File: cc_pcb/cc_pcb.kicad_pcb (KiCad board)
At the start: 2 copper layers, 134.7 x 117.2 mm, 66 parts, among them J1 Conn_02x05_Odd_Even, J10 AC-DC Converter, J2 Wi-Fi Module, J3 Controller (40Pin->SPI), J4 RFID Scanner, J5 4x4 Keypad, J6 SD Reader, J7 PS_Modules, J8 PS_Designed, J9 DC-DC Converter, Q1 2SC1941, SW1 SW_Push, U1 STM32F091RCTx, U2 LM393, U3 LD1117S33TR_SOT223, U4 LM2576T-5

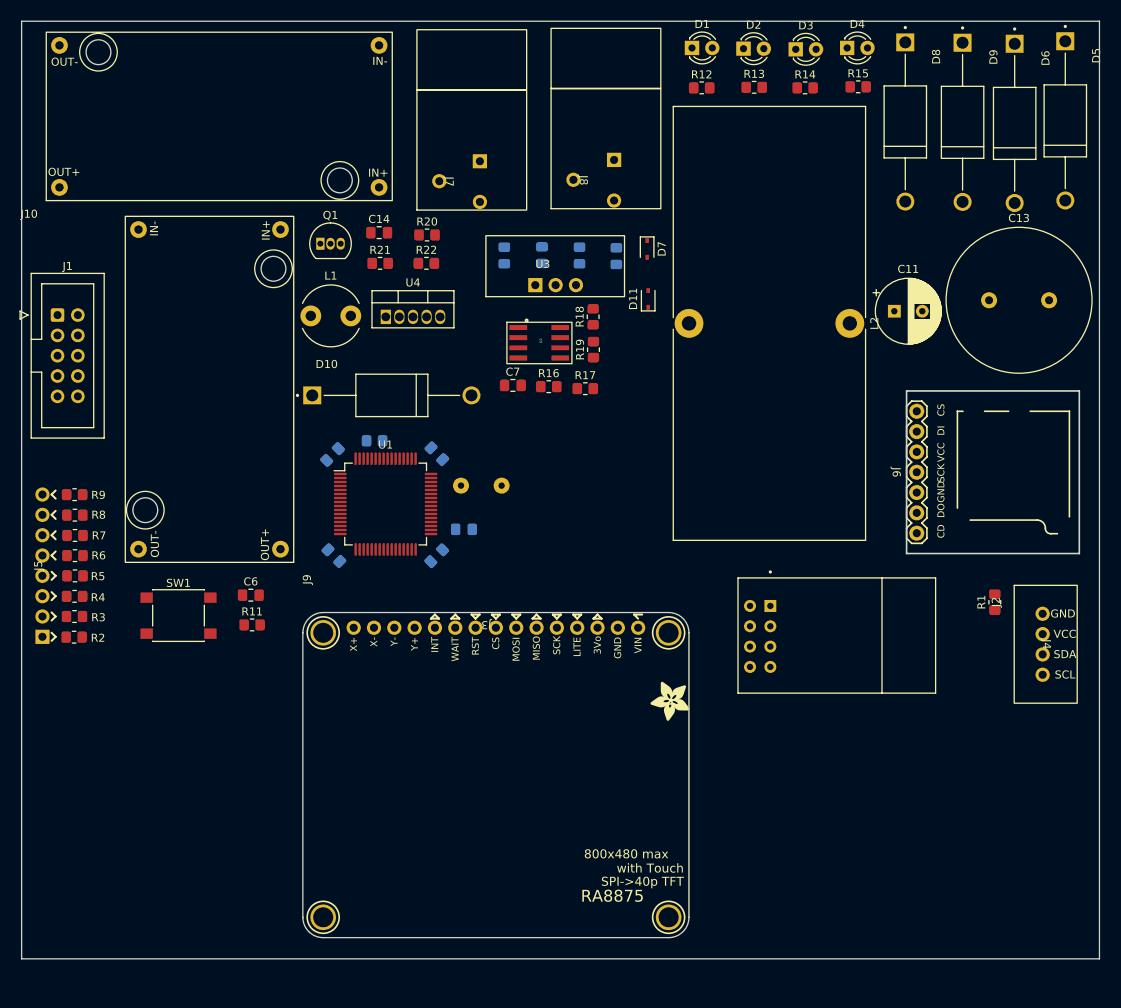
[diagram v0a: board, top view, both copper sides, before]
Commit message: RA8875 and ESP8266 updated footprints
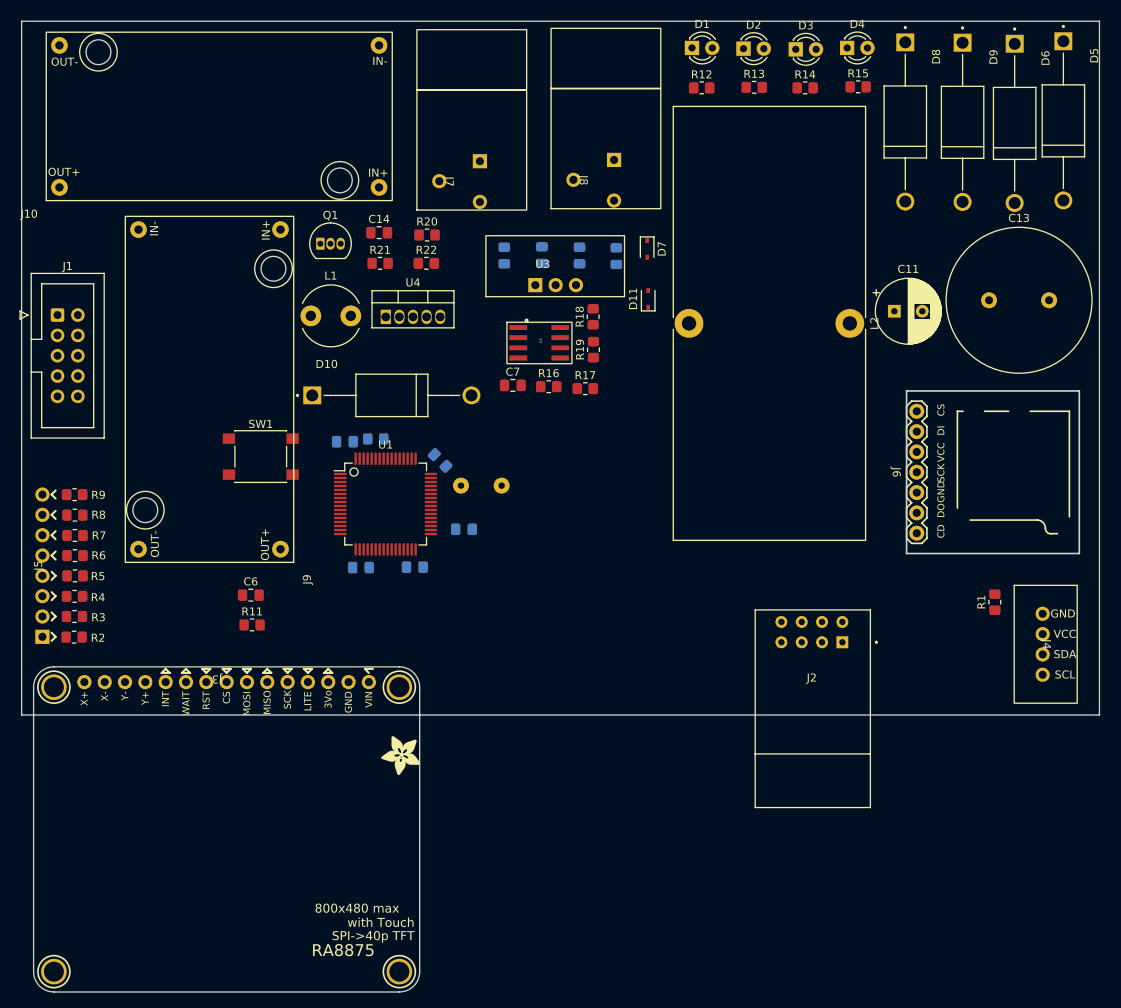
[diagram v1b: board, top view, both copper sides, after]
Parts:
- moved J3 34.3 mm to (105.3, 118.1)
- moved SW1 22.4 mm to (110.8, 90.8)
- moved J2 9.56 mm to (179.7, 122.3), turned to 180 degrees
- moved C1 3.69 mm to (123.3, 104.7), turned to 180 degrees
- moved C4 3.09 mm to (130.0, 104.6), turned to 180 degrees
- moved C2 2.22 mm to (121.3, 89.0), turned to 0 degrees
- moved C3 0.94 mm to (133.2, 91.3), turned to -45 degrees
- moved R10 0.28 mm to (125.1, 88.6)
- moved D5 0.24 mm to (211.1, 48.8)
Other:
- board size 134.7 x 117.2 mm -> 134.7 x 86.7 mm

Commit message: micro sd connector schematic/footprint, lm324 footprint
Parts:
- removed D10: 1N5822, imported_footprints:DIO_1N5822
- removed J4: RFID Scanner, imported_footprints:RFID_Reader_PCB
- removed Q1: 2SC1941, Package_TO_SOT_THT:TO-92_Inline
- added C15: 100nF, Capacitor_SMD:C_0805_2012Metric_Pad1.18x1.45mm_HandSolder, F.Cu at (35.2, 111.5)
- added C16: 33pF, Capacitor_SMD:C_0805_2012Metric_Pad1.18x1.45mm_HandSolder, F.Cu at (76.1, 27.0)
- added C17: 22uF, Capacitor_SMD:C_0805_2012Metric_Pad1.18x1.45mm_HandSolder, F.Cu at (71.3, 30.0)
- added C18: 100nF, Capacitor_SMD:C_0805_2012Metric_Pad1.18x1.45mm_HandSolder, F.Cu at (19.4, 120.5)
- added C19: .1uF, Capacitor_SMD:C_0805_2012Metric_Pad1.18x1.45mm_HandSolder, F.Cu at (76.1, 24.0)
- added C20: 10uF, Capacitor_SMD:C_0805_2012Metric_Pad1.18x1.45mm_HandSolder, F.Cu at (71.3, 24.0)
- added C21: .1uF, Capacitor_SMD:C_0805_2012Metric_Pad1.18x1.45mm_HandSolder, F.Cu at (71.3, 27.0)
- added J11: 2.8in SPI TFT Touch Display, imported_footprints:tft_2.8in_touch_display, F.Cu at (111.0, 117.3)
- added R23: 220k, Resistor_SMD:R_0805_2012Metric_Pad1.20x1.40mm_HandSolder, F.Cu at (71.3, 33.0)
- added R24: 30k, Resistor_SMD:R_0805_2012Metric_Pad1.20x1.40mm_HandSolder, F.Cu at (80.9, 24.0)
- added U6: RFID_Scanner, imported_footprints:RFID_Reader_PCB, F.Cu at (210.2, 114.5)
- C14: value 22uF -> 10uF
- FB1: footprint Ferrite_THT:LairdTech_28C0236-0JW-10 -> Resistor_SMD:R_0805_2012Metric_Pad1.20x1.40mm_HandSolder
- L1: value INDUCTOR -> 2.2uH
- R20: value 10k -> 100k
- R21: value 10k -> 11.3k
- U2: value LM393 -> LM324; footprint imported_footprints:LM393 -> imported_footprints:LM324
- U4: value LM2576T-5 -> TPS56325x; footprint Package_TO_SOT_THT:TO-220-5_Vertical -> imported_footprints:TPS56325x
- moved J2 82.8 mm to (248.6, 76.4)
- moved J3 58.4 mm to (163.6, 116.6)
- moved SW1 22.7 mm to (131.6, 81.8)
- moved FB1 20.8 mm to (123.8, 106.3), turned to 135 degrees
- moved C2 20.3 mm to (139.0, 98.9), turned to -135 degrees
- moved R10 17.5 mm to (136.5, 101.9), turned to 45 degrees
- moved C1 15.8 mm to (126.5, 89.2), turned to 45 degrees
- moved C5 15.5 mm to (120.8, 101.7), turned to 45 degrees
- moved C3 15.0 mm to (128.9, 105.7), turned to 180 degrees
- moved C4 13.5 mm to (121.8, 94.0), turned to 45 degrees
- moved R1 8.28 mm to (203.4, 117.2)
- moved U1 3.54 mm to (129.9, 97.0), turned to -135 degrees
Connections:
- net /BOOT0 renamed PF11
- net /CD renamed /SD_CD
- net /GPIO-0 renamed /ESP_GPIO-0
- net /GPIO-2 renamed /ESP_GPIO-2
- net /LITE renamed /7_LITE
- net /WAIT renamed /7_WAIT
- C1 pad 1: +3V3 -> 3.3V
- C1 pad 2: GND -> 3.3V
- C11 pad 2: 7.5_GND -> 3.3V
- C13 pad 2: 7.5_GND -> 3.3V
- C14 pad 1: +3V3 -> +7.5V
- C14 pad 2: GND -> 3.3V
- C2 pad 1: +3V3 -> 3.3V
- C2 pad 2: GND -> 3.3V
- C3 pad 1: +3V3 -> 3.3V
- C3 pad 2: GND -> 3.3V
- C4 pad 1: +3V3 -> 3.3V
- C4 pad 2: GND -> 3.3V
- C5 pad 2: GND -> 3.3V
- C6 pad 2: GND -> 3.3V
- C8 pad 1: +3V3 -> +5V
- C9 pad 1: +3V3 -> +5V
- D1 pad 1: GND -> 3.3V
- D11 pad 1: +3V3 -> 3.3V
- D2 pad 1: GND -> 3.3V
- D3 pad 1: GND -> 3.3V
- D4 pad 1: GND -> 3.3V
- D6 pad 2: 7.5_GND -> Net-(D6-Pad2)
- D7 pad 1: GND -> 3.3V
- D9 pad 2: 7.5_GND -> Net-(D6-Pad2)
- FB1 pad 1: +3V3 -> 3.3V
- J1 pad 3: GND -> 3.3V
- J1 pad 4: GND -> 3.3V
- J10 pad 4: GND -> 3.3V
- J2 pad 1: GND -> 3.3V
- J2 pad 2: PA9 -> PA10
- J2 pad 4: +3V3 -> /ESP_CH_EN
- J2 pad 6: PB11 -> /ESP_RST
- J2 pad 8: +3V3 -> 3.3V
- J3 pad 1: +3V3 -> 3.3V
- J3 pad 2: GND -> 3.3V
- J3 pad 5: PB10 -> PB3
- J6 pad 3: GND -> 3.3V
- J6 pad 5: +3V3 -> 3.3V
- J6 pad 7: PB8 -> PB9
- J9 pad 2: 7.5_GND -> 3.3V
- J9 pad 3: +3V3 -> +5V
- J9 pad 4: GND -> 3.3V
- L1 pad 2: +3V3 -> +5V
- R1 pad 1: PA9 -> Net-(R1-Pad1)
- R10 pad 2: GND -> 3.3V
- R11 pad 1: +3V3 -> 3.3V
- R16 pad 2: GND -> 3.3V
- R17 pad 2: GND -> 3.3V
- R19 pad 1: +3V3 -> +5V
- R20 pad 1: Net-(Q1-Pad3) -> +7.5V
- R20 pad 2: +7.5V -> Net-(R20-Pad2)
- R21 pad 1: Net-(Q1-Pad3) -> Net-(R20-Pad2)
- R21 pad 2: GND -> 3.3V
- R22 pad 2: Net-(Q1-Pad2) -> +5V
- SW1 pad 1: GND -> 3.3V
- U1 pad 1: +3V3 -> 3.3V
- U1 pad 12: GND -> 3.3V
- U1 pad 18: GND -> 3.3V
- U1 pad 19: +3V3 -> 3.3V
- U1 pad 31: GND -> 3.3V
- U1 pad 32: +3V3 -> 3.3V
- U1 pad 35: /PB14 -> PB14
- U1 pad 43: /PA10 -> PA10
- U1 pad 47: GND -> 3.3V
- U1 pad 48: +3V3 -> 3.3V
- U1 pad 54: PA9 -> PD2
- U1 pad 55: PB10 -> PB3
- U1 pad 59: /PB7 -> PB7
- U1 pad 62: PB8 -> PB9
- U1 pad 63: GND -> 3.3V
- U1 pad 64: +3V3 -> 3.3V
- U2 pad 4: (no net) -> +5V
- U3 pad 3: +3V3 -> +5V
- U4 pad 1: Net-(Q1-Pad2) -> +7.5V
- U4 pad 3: GND -> 3.3V
- U4 pad 5: GND -> Net-(R20-Pad2)

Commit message: initial PCB components, traces laid out with DRC passed
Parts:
- removed C21: .1uF, Capacitor_SMD:C_0805_2012Metric_Pad1.18x1.45mm_HandSolder
- removed J10: AC-DC Converter, imported_footprints:7.5Vdc-5Vdc_buck_converter
- removed J11: 2.8in SPI TFT Touch Display, imported_footprints:tft_2.8in_touch_display
- removed J8: PS_Designed, imported_footprints:barrel_jack_adapter
- removed J9: DC-DC Converter, imported_footprints:7.5Vdc-5Vdc_buck_converter
- added D10: 1N5822, imported_footprints:DIO_1N5822, F.Cu at (198.3, 95.7)
- added D12: 1N5822, imported_footprints:DIO_1N5822, F.Cu at (189.9, 74.5)
- added D13: 1N5822, imported_footprints:DIO_1N5822, F.Cu at (196.7, 74.6)
- added D14: 1N5822, imported_footprints:DIO_1N5822, F.Cu at (175.0, 73.9)
- added D15: 1N5822, imported_footprints:DIO_1N5822, F.Cu at (174.9, 66.1)
- added H1: MountingHole, MountingHole:MountingHole_8.4mm_M8, F.Cu at (204.0, 129.0)
- added H10: MountingHole, MountingHole:MountingHole_2.2mm_M2_ISO7380, F.Cu at (101.9, 90.5)
- added H2: MountingHole, MountingHole:MountingHole_8.4mm_M8, F.Cu at (82.0, 130.0)
- added H3: MountingHole, MountingHole:MountingHole_8.4mm_M8, F.Cu at (83.0, 49.0)
- added H4: MountingHole, MountingHole:MountingHole_8.4mm_M8, F.Cu at (204.0, 49.0)
- added H5: MountingHole, MountingHole:MountingHole_2.2mm_M2_ISO7380, F.Cu at (148.6, 102.0)
- added H6: MountingHole, MountingHole:MountingHole_2.2mm_M2_ISO7380, F.Cu at (191.8, 102.0)
- added H7: MountingHole, MountingHole:MountingHole_2.2mm_M2_ISO7380, F.Cu at (191.8, 137.6)
- added H8: MountingHole, MountingHole:MountingHole_2.2mm_M2_ISO7380, F.Cu at (148.7, 137.6)
- added H9: MountingHole, MountingHole:MountingHole_2.2mm_M2_ISO7380, F.Cu at (117.9, 60.4)
- added J4: DC-DC_JUMPER, Connector_PinSocket_1.27mm:PinSocket_2x03_P1.27mm_Vertical, F.Cu at (137.4, 42.4)
- added R25: .33M, Resistor_SMD:R_0805_2012Metric_Pad1.20x1.40mm_HandSolder, F.Cu at (184.1, 93.7)
- added R26: 10k, Resistor_SMD:R_0805_2012Metric_Pad1.20x1.40mm_HandSolder, F.Cu at (143.3, 89.0)
- added R27: 10k, Resistor_SMD:R_0805_2012Metric_Pad1.20x1.40mm_HandSolder, F.Cu at (176.9, 79.1)
- added R28: 300, Resistor_SMD:R_0805_2012Metric_Pad1.20x1.40mm_HandSolder, F.Cu at (131.6, 85.9)
- added U5: 74HC14, imported_footprints:SN74HC14N, F.Cu at (170.5, 87.3)
- added U7: LD1117S33TR_SOT223, imported_footprints:5-3.3_buck_converter, F.Cu at (108.7, 109.8)
- added U8: TPS56325x, Package_TO_SOT_SMD:SOT-563, F.Cu at (137.7, 89.1)
- added U9: 4N28, Package_DIP:DIP-6_W7.62mm, F.Cu at (184.6, 88.3)
- C11: value 100m -> .1uF; footprint Capacitor_THT:CP_Radial_D8.0mm_P3.50mm -> Capacitor_SMD:C_0805_2012Metric_Pad1.18x1.45mm_HandSolder; moved to B.Cu
- C13: value 1m -> 10uF; footprint Capacitor_THT:C_Radial_D18.0mm_H35.5mm_P7.50mm -> Capacitor_SMD:C_0805_2012Metric_Pad1.18x1.45mm_HandSolder
- C14, C20: value 10uF -> 100nF
- C15: value 100nF -> .1uF; moved to B.Cu
- C17: value 22uF -> 100m; footprint Capacitor_SMD:C_0805_2012Metric_Pad1.18x1.45mm_HandSolder -> Capacitor_THT:CP_Radial_D8.0mm_P3.50mm
- C18: value 100nF -> 1m; footprint Capacitor_SMD:C_0805_2012Metric_Pad1.18x1.45mm_HandSolder -> Capacitor_THT:C_Radial_D18.0mm_H35.5mm_P7.50mm
- C19, C9: value .1uF -> 22uF
- C8: value 22uF -> .1uF; moved to F.Cu
- D1: value LED -> LED_RED; footprint LED_THT:LED_D3.0mm -> LED_SMD:LED_0805_2012Metric_Pad1.15x1.40mm_HandSolder
- D11: value BAT60JFILM -> 1N5822; footprint Diode_SMD:D_SOD-323 -> imported_footprints:DIO_1N5822
- D2: value LED -> LED_YELLOW; footprint LED_THT:LED_D3.0mm -> LED_SMD:LED_0805_2012Metric_Pad1.15x1.40mm_HandSolder
- D3: value LED -> LED_GREEN; footprint LED_THT:LED_D3.0mm -> LED_SMD:LED_0805_2012Metric_Pad1.15x1.40mm_HandSolder
- D5, D6: value 1N5822 -> LED; footprint imported_footprints:DIO_1N5822 -> LED_THT:LED_D3.0mm
- D7: value BAT60JFILM -> LED; footprint Diode_SMD:D_SOD-323 -> LED_THT:LED_D3.0mm
- D8, D9: value 1N5822 -> BAT60JFILM; footprint imported_footprints:DIO_1N5822 -> Diode_SMD:D_SOD-323
- J2: value Wi-Fi Module -> Micro_SD_Card_Det_Hirose_DM3AT; footprint imported_footprints:XCVR_ESP8266-01_ESP-01 -> Connector_Card:microSD_HC_Hirose_DM3AT-SF-PEJM5
- J3: value Controller (40Pin->SPI) -> 4x4 Keypad; footprint imported_footprints:RA8875_TFT_Breakout -> imported_footprints:4x4_keypad
- J5: value 4x4 Keypad -> PS_WIRES; footprint imported_footprints:4x4_keypad -> imported_footprints:PS_2_Wire
- J6: value SD Reader -> PS_BJ; footprint imported_footprints:Micro_SD_card_reader -> imported_footprints:barrel_jack_adapter
- J7: value PS_Modules -> DC-DC Converter; footprint imported_footprints:barrel_jack_adapter -> imported_footprints:7.5Vdc-5Vdc_buck_converter
- L1: value 2.2uH -> 1m; footprint Inductor_THT:L_Radial_D7.5mm_P5.00mm_Fastron_07P -> Inductor_THT:L_Toroid_Vertical_L54.0mm_W23.8mm_P20.10mm_Bourns_5700
- L2: value 1m -> 2.2uH; footprint Inductor_THT:L_Toroid_Vertical_L54.0mm_W23.8mm_P20.10mm_Bourns_5700 -> Inductor_THT:L_Radial_D7.5mm_P5.00mm_Fastron_07P
- R10: value 100K -> 1k; moved to F.Cu
- R11: value 100K -> 1k
- R12, R13: value 150 -> 1k
- R14: value 150 -> 100K; moved to B.Cu
- R16, R17: value 10k -> 150
- R18: value 330k -> 150
- R19: value 3.3k -> 100k
- R2, R5: value 1k -> 100K
- R20: value 100k -> 11k
- R21: value 11.3k -> 820
- R22: value 10k -> 68
- R3: value 1k -> 10k
- R4: value 1k -> 2k
- U1: value STM32F091RCTx -> ESP8266; footprint Package_QFP:LQFP-64_10x10mm_P0.5mm -> imported_footprints:XCVR_ESP8266-01_ESP-01
- U2: value LM324 -> 7in_display_controller; footprint imported_footprints:LM324 -> imported_footprints:RA8875_TFT_Breakout
- U3: value LD1117S33TR_SOT223 -> RFID_Scanner; footprint imported_footprints:5-3.3_buck_converter -> imported_footprints:RFID_Reader_PCB
- U4: value TPS56325x -> TFT_2.8IN_DISPLAY; footprint imported_footprints:TPS56325x -> imported_footprints:tft_2.8in_touch_display
- U6: value RFID_Scanner -> STM32F091RCTx; footprint imported_footprints:RFID_Reader_PCB -> Package_QFP:LQFP-64_10x10mm_P0.5mm
- moved J2 167.8 mm to (81.2, 87.5), turned to -90 degrees
- moved C15 138.1 mm to (171.2, 87.5), turned to 45 degrees
- moved J5 130.4 mm to (213.3, 92.4)
- moved C18 129.3 mm to (140.8, 76.2), turned to 45 degrees
- moved D5 124.2 mm to (88.0, 65.0), turned to 0 degrees
- moved D9 120.1 mm to (95.0, 110.0), turned to 0 degrees
- moved D6 119.0 mm to (88.0, 71.0), turned to 0 degrees
- moved D8 112.1 mm to (95.0, 106.3), turned to 0 degrees
- moved R13 107.5 mm to (81.1, 101.3)
- moved R12 103.3 mm to (81.1, 103.8)
- moved D4 97.3 mm to (88.7, 59.0)
- moved C19 96.4 mm to (126.5, 106.2), turned to 180 degrees
- moved C20 96.1 mm to (126.6, 102.6), turned to 180 degrees
- moved C16 96.0 mm to (142.9, 95.9), turned to 90 degrees
- moved C17 94.3 mm to (156.5, 70.2), turned to 45 degrees
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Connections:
- C1 pad 1: 3.3V -> +3V3
- C1 pad 2: 3.3V -> GND
- C10 pad 1: Net-(C10-Pad1) -> +5V
- C11 pad 2: 3.3V -> Net-(C10-Pad2)
- C12 pad 1: Net-(C10-Pad1) -> Net-(C11-Pad1)
- C13 pad 1: Net-(C11-Pad1) -> DC_DES
- C13 pad 2: 3.3V -> GND
- C14 pad 1: +7.5V -> DC_DES
- C14 pad 2: 3.3V -> GND
- C15 pad 1: +7.5V -> +3V3
- C15 pad 2: 3.3V -> GND
- C17 pad 1: +5V -> +9V
- C17 pad 2: 3.3V -> 9_GND
- C18 pad 1: +5V -> +9V
- C18 pad 2: 3.3V -> 9_GND
- C19 pad 1: 3.3V -> +5V
- C19 pad 2: 3.3V -> GND
- C2 pad 1: 3.3V -> +3V3
- C2 pad 2: 3.3V -> GND
- C20 pad 1: 3.3V -> +5V
- C20 pad 2: 3.3V -> GND
- C3 pad 1: 3.3V -> +3V3
- C3 pad 2: 3.3V -> GND
- C4 pad 1: 3.3V -> +3V3
- C4 pad 2: 3.3V -> GND
- C5 pad 2: 3.3V -> GND
- C6 pad 1: /NRST -> GND
- C6 pad 2: 3.3V -> +3V3
- C7 pad 1: VAC_designs -> GND
- C7 pad 2: Net-(U2-Pad2) -> +3V3
- C8 pad 1: +5V -> /NRST
- C8 pad 2: Net-(C10-Pad2) -> GND
- D1 pad 1: 3.3V -> GND
- D11 pad 1: 3.3V -> Net-(D10-Pad1)
- D11 pad 2: Net-(C10-Pad1) -> VAC_GND
- D2 pad 1: 3.3V -> GND
- D3 pad 1: 3.3V -> GND
- D4 pad 1: 3.3V -> GND
- D5 pad 1: Net-(C11-Pad1) -> GND
- D5 pad 2: VAC_designs -> Net-(D5-Pad2)
- D6 pad 1: VAC_designs -> GND
- D7 pad 1: 3.3V -> GND
- D7 pad 2: Net-(C10-Pad2) -> Net-(D7-Pad2)
- D8 pad 1: Net-(C11-Pad1) -> GND
- D8 pad 2: VAC_designs_gnd -> Net-(C10-Pad2)
- D9 pad 1: VAC_designs_gnd -> +3V3
- D9 pad 2: Net-(D6-Pad2) -> Net-(C11-Pad1)
- FB1 pad 1: 3.3V -> +3V3
- J1 pad 3: 3.3V -> GND
- J1 pad 4: 3.3V -> GND
- J2 pad 1: 3.3V -> unconnected-(J2-Pad1)
- J2 pad 2: PA10 -> PB9
- J2 pad 3: /ESP_GPIO-2 -> PC3
- J2 pad 4: /ESP_CH_EN -> +3V3
- J2 pad 5: /ESP_GPIO-0 -> PB10
- J2 pad 6: /ESP_RST -> GND
- J2 pad 7: PA9 -> PC2
- J2 pad 8: 3.3V -> unconnected-(J2-Pad8)
- J3 pad 1: 3.3V -> Net-(J3-Pad1)
- J3 pad 2: 3.3V -> Net-(J3-Pad2)
- J3 pad 3: /3Vo -> Net-(J3-Pad3)
- J3 pad 4: /7_LITE -> Net-(J3-Pad4)
- J3 pad 5: PB3 -> Net-(J3-Pad5)
- J3 pad 6: PB4 -> Net-(J3-Pad6)
- J3 pad 7: PB5 -> Net-(J3-Pad7)
- J3 pad 8: PB8 -> Net-(J3-Pad8)
- J5 pad 1: Net-(J5-Pad1) -> VAC
- J5 pad 2: Net-(J5-Pad2) -> VAC_GND
- J6 pad 1: /SD_CD -> VAC
- J6 pad 2: PC2 -> VAC_GND
- J6 pad 3: 3.3V -> unconnected-(J6-Pad3)
- J7 pad 1: VAC_designs -> DC_MOD
- J7 pad 2: VAC_modules_gnd -> DC_MOD_GND
- J7 pad 3: /OTHER -> +5V
- L1 pad 1: Net-(L1-Pad1) -> Net-(D12-Pad1)
- L1 pad 2: +5V -> +9V
- L2 pad 1: Net-(C11-Pad1) -> Net-(L2-Pad1)
- L2 pad 2: +7.5V -> +5V
- R10 pad 1: PF11 -> Net-(J3-Pad5)
- R10 pad 2: 3.3V -> PC7
- R11 pad 1: 3.3V -> Net-(J3-Pad6)
- R11 pad 2: /NRST -> PC6
- R12 pad 1: PA5 -> Net-(J3-Pad7)
- R12 pad 2: Net-(D1-Pad2) -> PC5
- R13 pad 1: PA6 -> Net-(J3-Pad8)
- R13 pad 2: Net-(D2-Pad2) -> PC4
- R14 pad 1: PA7 -> PF11
- R14 pad 2: Net-(D3-Pad2) -> GND
- R15 pad 1: PA8 -> PA5
- R16 pad 1: Net-(U2-Pad2) -> PA6
- R16 pad 2: 3.3V -> Net-(D5-Pad2)
- R17 pad 1: Net-(U2-Pad3) -> PA7
- R17 pad 2: 3.3V -> Net-(D6-Pad2)
- R18 pad 1: Net-(U2-Pad3) -> PA8
- R18 pad 2: PB0 -> Net-(D7-Pad2)
- R19 pad 1: +5V -> DC_DES
- R19 pad 2: PB0 -> Net-(R19-Pad2)
- R2 pad 1: Net-(J5-Pad1) -> +9V
- R2 pad 2: PC11 -> Net-(D1-Pad2)
- R20 pad 1: +7.5V -> Net-(R19-Pad2)
- R21 pad 1: Net-(R20-Pad2) -> Net-(R21-Pad1)
- R21 pad 2: 3.3V -> Net-(D10-Pad1)
- R22 pad 2: +5V -> Net-(R21-Pad1)
- R24 pad 1: 3.3V -> GND
- R3 pad 1: Net-(J5-Pad2) -> +5V
- R3 pad 2: PC10 -> Net-(D2-Pad2)
- R4 pad 1: Net-(J5-Pad3) -> +3V3
- R4 pad 2: PC9 -> Net-(D3-Pad2)
- R5 pad 1: Net-(J5-Pad4) -> +3V3
- R5 pad 2: PC8 -> /NRST
- R6 pad 1: Net-(J5-Pad5) -> Net-(J3-Pad1)
- R6 pad 2: PC7 -> PC11
- R7 pad 1: Net-(J5-Pad6) -> Net-(J3-Pad2)
- R7 pad 2: PC6 -> PC10
- R8 pad 1: Net-(J5-Pad7) -> Net-(J3-Pad3)
- R8 pad 2: PC5 -> PC9
- R9 pad 1: Net-(J5-Pad8) -> Net-(J3-Pad4)
- R9 pad 2: PC4 -> PC8
- SW1 pad 1: 3.3V -> GND
- U1 pad 1: 3.3V -> GND
- U1 pad 2: /PC13 -> PA10
- U1 pad 3: /PC14 -> unconnected-(U1-Pad3)
- U1 pad 4: /PC15 -> unconnected-(U1-Pad4)
- U1 pad 5: /PF0 -> unconnected-(U1-Pad5)
- U1 pad 6: /PF1 -> unconnected-(U1-Pad6)
- U1 pad 7: /NRST -> PA9
- U1 pad 8: /PC0 -> +3V3
- U2 pad 1: PB0 -> +3V3
- U2 pad 10: (no net) -> unconnected-(U2-Pad10)
- U2 pad 11: 3.3V -> PA0
- U2 pad 12: (no net) -> PA1
- U2 pad 13: (no net) -> PA2
- U2 pad 14: (no net) -> PA3
- U2 pad 2: Net-(U2-Pad2) -> GND
- U2 pad 3: Net-(U2-Pad3) -> unconnected-(U2-Pad3)
- U2 pad 4: +5V -> unconnected-(U2-Pad4)
- U2 pad 5: (no net) -> PB3
- U2 pad 6: (no net) -> PB4
- U2 pad 7: (no net) -> PB5
- U2 pad 8: (no net) -> PB8
- U2 pad 9: (no net) -> PB11
- U3 pad 1: Net-(C10-Pad2) -> GND
- U3 pad 2: Net-(C10-Pad1) -> +5V
- U3 pad 3: +5V -> PD2
- U4 pad 1: +7.5V -> +3V3
- U4 pad 2: Net-(L1-Pad1) -> GND
- U4 pad 3: 3.3V -> PB8
- U4 pad 4: Net-(R22-Pad1) -> PB11
- U4 pad 5: Net-(R20-Pad2) -> PB14
- U4 pad 6: Net-(C16-Pad2) -> PB5
- U6 pad 1: 3.3V -> +3V3
- U6 pad 2: +5V -> /PC13
- U6 pad 3: PD2 -> /PC14
- U6 pad 4: Net-(R1-Pad1) -> /PC15
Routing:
- net +5V: track 0.00 -> 243.0 mm, vias 0 -> 4
- net GND: track 0.00 -> 125.6 mm, vias 0 -> 16
- net PB4: track 0.00 -> 115.2 mm, vias 0 -> 1
- net PA9: track 0.00 -> 114.6 mm, vias 0 -> 1
- net PB3: track 0.00 -> 111.2 mm, vias 0 -> 1
- net PB5: track 0.00 -> 109.2 mm, vias 0 -> 2
- net PC11: track 0.00 -> 106.7 mm
- net PC10: track 0.00 -> 105.1 mm
- net PA0: track 0.00 -> 104.6 mm, vias 0 -> 3
- net PA10: track 0.00 -> 100.6 mm, vias 0 -> 1
- net PC9: track 0.00 -> 96.4 mm
- net /PA14: track 0.00 -> 96.1 mm, vias 0 -> 1
- net PC8: track 0.00 -> 95.9 mm
- net PC7: track 0.00 -> 94.6 mm
- net /PA13: track 0.00 -> 93.4 mm, vias 0 -> 1
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- added copper zone on B.Cu, net +3V3
- added copper zone on F.Cu, net GND
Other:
- board size 134.7 x 86.7 mm -> 145.2 x 105.1 mm

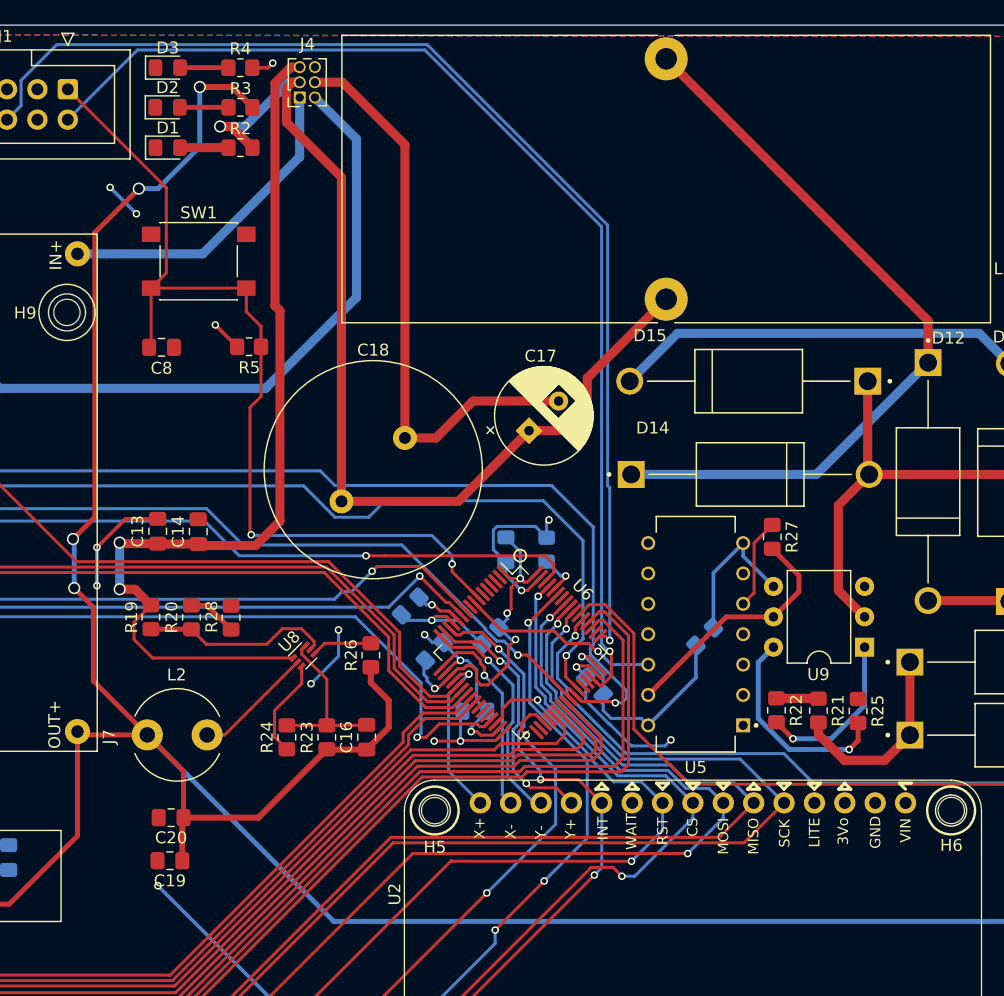
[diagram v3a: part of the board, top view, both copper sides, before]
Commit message: 1:1 footprint changes and layout modded to follow rules
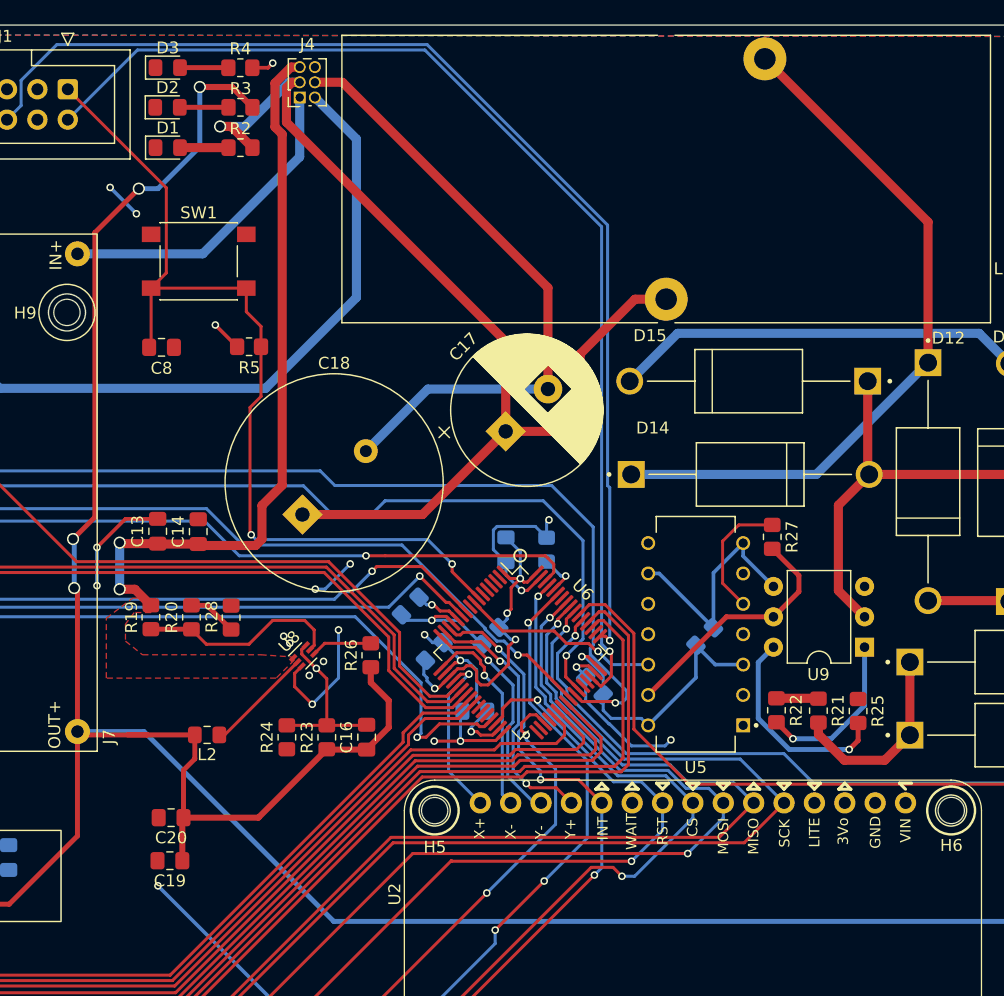
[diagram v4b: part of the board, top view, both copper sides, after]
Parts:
- C17: value 100m -> 1m; footprint Capacitor_THT:CP_Radial_D8.0mm_P3.50mm -> Capacitor_THT:CP_Radial_D12.5mm_P5.00mm
- C18: value 1m -> 10m
- L2: footprint Inductor_THT:L_Radial_D7.5mm_P5.00mm_Fastron_07P -> Inductor_SMD:L_0805_2012Metric_Pad1.15x1.40mm_HandSolder
- moved C18 3.45 mm to (137.6, 77.3)
- moved C17 1.95 mm to (154.6, 70.3)
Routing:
- net DC_DES: track 78.2 -> 61.0 mm
- net GND: track 125.6 -> 134.2 mm, vias 16 -> 18
- net +5V: track 243.0 -> 251.0 mm
- net +3V3: track 81.3 -> 89.0 mm
- net +9V: track 84.8 -> 90.1 mm
- net 9_GND: track 48.3 -> 52.5 mm
- net Net-(D12-Pad1): track 63.2 -> 59.8 mm
- net Net-(R19-Pad2): track 16.0 -> 17.1 mm
- net Net-(L2-Pad1): track 10.1 -> 9.04 mm
- net Net-(C16-Pad2): vias 0 -> 1
- net (no net): vias 0 -> 4
- added copper zone on F.Cu, net DC_DES
